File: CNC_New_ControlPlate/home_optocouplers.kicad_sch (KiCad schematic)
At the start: 17 parts

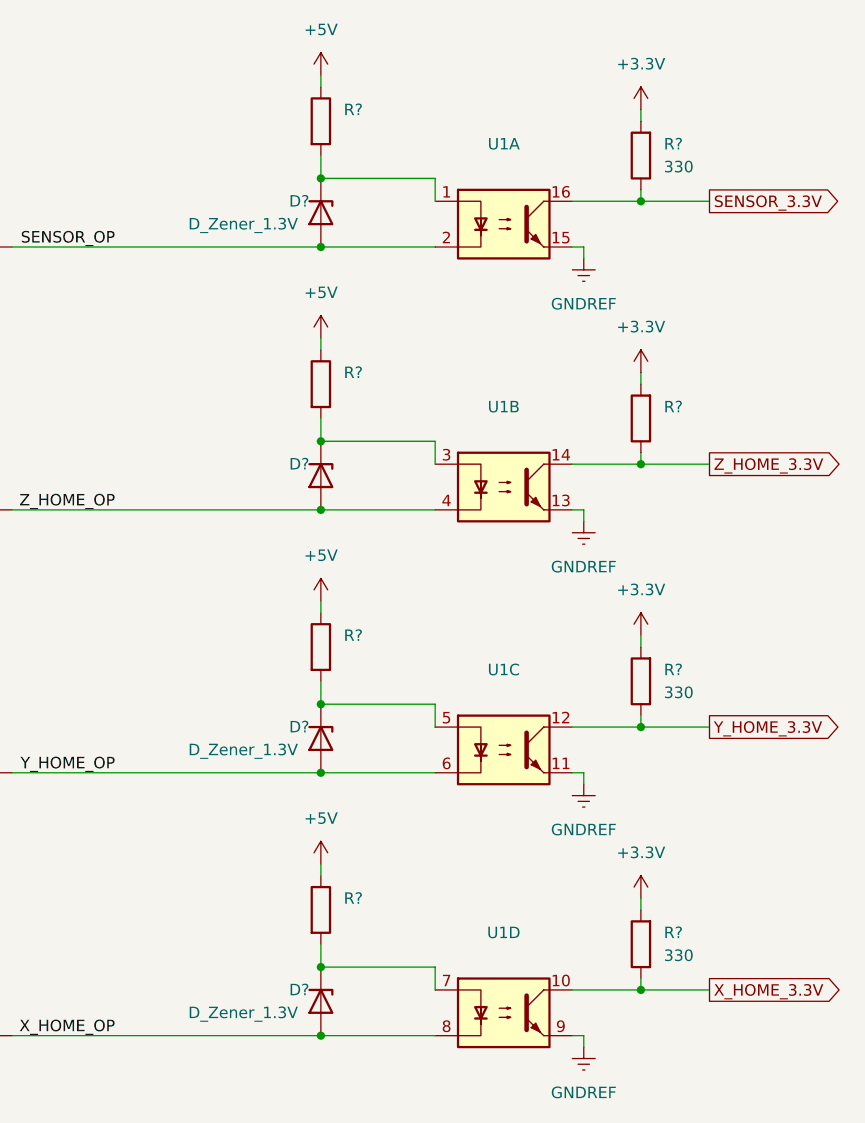
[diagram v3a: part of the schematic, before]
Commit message: Add spindel sch
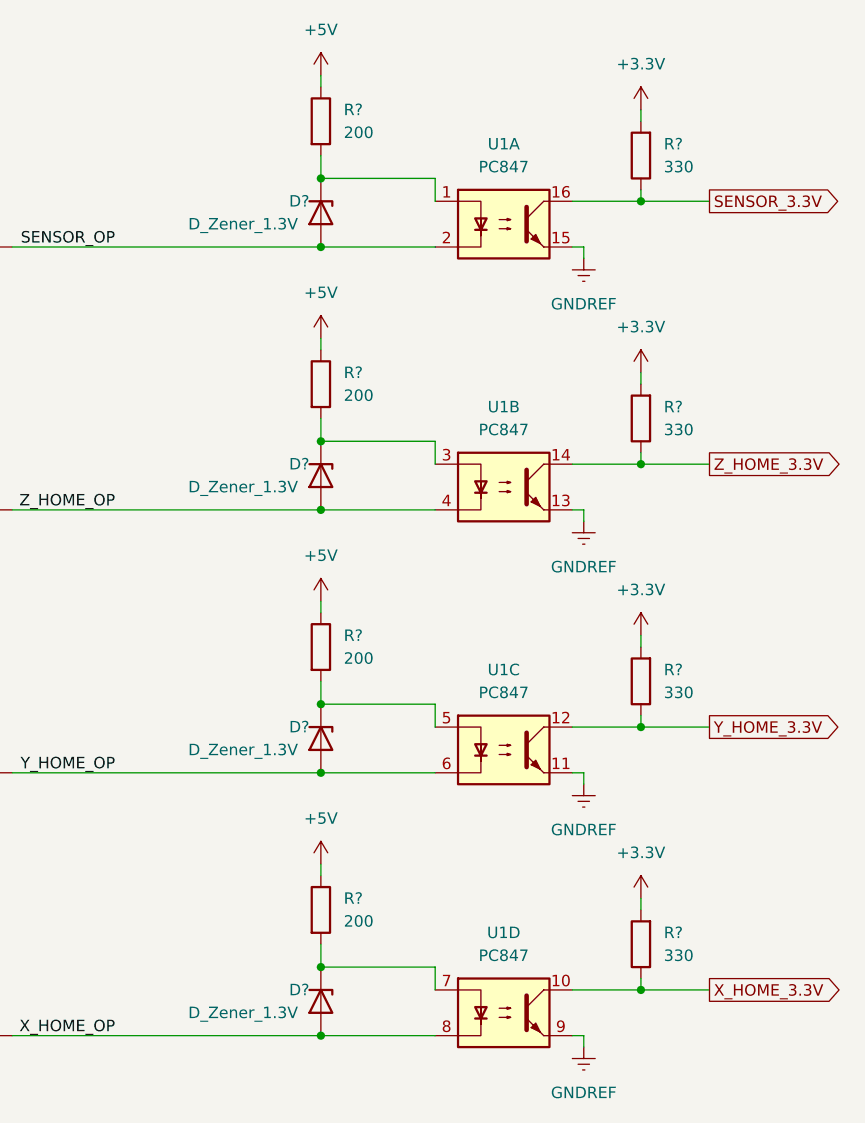
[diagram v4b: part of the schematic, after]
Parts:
- D?: value (none) -> D_Zener_1.3V; footprint (none) -> Diode_SMD:D_0603_1608Metric
- FB2: value (none) -> FerriteBead; footprint (none) -> Resistor_SMD:R_0603_1608Metric
- R? (x2): value (none) -> 200
- R? (x2): value (none) -> 200; footprint (none) -> Resistor_SMD:R_0603_1608Metric
- R?: value (none) -> 330; footprint (none) -> Resistor_SMD:R_0603_1608Metric
- U1: value (none) -> PC847; footprint (none) -> Package_DIP:DIP-16_W7.62mm_Socket_LongPads
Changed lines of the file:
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@@
       (effects (font (size 1.27 1.27)) (justify left))
     )
-    (property "Value" "" (id 1) (at 156.21 96.5199 0)
+    (property "Value" "200" (id 1) (at 156.21 96.5199 0)
       (effects (font (size 1.27 1.27)) (justify left))
     )
@@
       (effects (font (size 1.27 1.27)) (justify right))
     )
-    (property "Value" "" (id 1) (at 151.13 77.47 90)
-      (effects (font (size 1.27 1.27)) (justify right))
-    )
-    (property "Footprint" "" (id 2) (at 153.67 76.2 0)
+    (property "Value" "D_Zener_1.3V" (id 1) (at 151.13 77.47 90)
+      (effects (font (size 1.27 1.27)) (justify right))
+    )
+    (property "Footprint" "Diode_SMD:D_0603_1608Metric" (id 2) (at 153.67 76.2 0)
       (effects (font (size 1.27 1.27)) hide)
     )
@@
       (effects (font (size 1.27 1.27)) (justify left))
     )
-    (property "Value" "" (id 1) (at 156.21 38.0999 0)
-      (effects (font (size 1.27 1.27)) (justify left))
-    )
-    (property "Footprint" "" (id 2) (at 151.892 36.83 90)
+    (property "Value" "200" (id 1) (at 156.21 38.0999 0)
+      (effects (font (size 1.27 1.27)) (justify left))
+    )
+    (property "Footprint" "Resistor_SMD:R_0603_1608Metric" (id 2) (at 151.892 36.83 90)
       (effects (font (size 1.27 1.27)) hide)
     )
@@
     (in_bom yes) (on_board yes) (fields_autoplaced)
     (property "Reference" "U1" (id 0) (at 173.99 39.37 0))
-    (property "Value" "" (id 1) (at 173.99 41.91 0))
-    (property "Footprint" "" (id 2) (at 168.91 53.34 0)
+    (property "Value" "PC847" (id 1) (at 173.99 41.91 0))
+    (property "Footprint" "Package_DIP:DIP-16_W7.62mm_Socket_LongPads" (id 2) (at 168.91 53.34 0)
       (effects (font (size 1.27 1.27) italic) (justify left) hide)
     )
@@
       (effects (font (size 1.27 1.27)) (justify left))
     )
-    (property "Value" "" (id 1) (at 156.21 67.3099 0)
-      (effects (font (size 1.27 1.27)) (justify left))
-    )
-    (property "Footprint" "" (id 2) (at 151.892 66.04 90)
+    (property "Value" "200" (id 1) (at 156.21 67.3099 0)
+      (effects (font (size 1.27 1.27)) (justify left))
+    )
+    (property "Footprint" "Resistor_SMD:R_0603_1608Metric" (id 2) (at 151.892 66.04 90)
       (effects (font (size 1.27 1.27)) hide)
     )
@@
       (effects (font (size 1.27 1.27)) (justify left))
     )
-    (property "Value" "" (id 1) (at 156.21 125.7299 0)
+    (property "Value" "200" (id 1) (at 156.21 125.7299 0)
       (effects (font (size 1.27 1.27)) (justify left))
     )
@@
     (in_bom yes) (on_board yes) (fields_autoplaced)
     (property "Reference" "U1" (id 0) (at 173.99 127 0))
-    (property "Value" "" (id 1) (at 173.99 129.54 0))
-    (property "Footprint" "" (id 2) (at 168.91 140.97 0)
+    (property "Value" "PC847" (id 1) (at 173.99 129.54 0))
+    (property "Footprint" "Package_DIP:DIP-16_W7.62mm_Socket_LongPads" (id 2) (at 168.91 140.97 0)
       (effects (font (size 1.27 1.27) italic) (justify left) hide)
     )
@@
     (in_bom yes) (on_board yes)
     (property "Reference" "U1" (id 0) (at 173.99 97.79 0))
-    (property "Value" "" (id 1) (at 173.99 100.33 0))
-    (property "Footprint" "" (id 2) (at 168.91 111.76 0)
+    (property "Value" "PC847" (id 1) (at 173.99 100.33 0))
+    (property "Footprint" "Package_DIP:DIP-16_W7.62mm_Socket_LongPads" (id 2) (at 168.91 111.76 0)
       (effects (font (size 1.27 1.27) italic) (justify left) hide)
     )
@@
       (effects (font (size 1.27 1.27)) (justify right))
     )
-    (property "Value" "" (id 1) (at 191.77 71.1199 0)
-      (effects (font (size 1.27 1.27)) (justify right))
-    )
-    (property "Footprint" "" (id 2) (at 191.008 69.85 90)
+    (property "Value" "330" (id 1) (at 191.77 71.1199 0)
+      (effects (font (size 1.27 1.27)) (justify right))
+    )
+    (property "Footprint" "Resistor_SMD:R_0603_1608Metric" (id 2) (at 191.008 69.85 90)
       (effects (font (size 1.27 1.27)) hide)
     )
@@
     (in_bom yes) (on_board yes) (fields_autoplaced)
     (property "Reference" "U1" (id 0) (at 173.99 68.58 0))
-    (property "Value" "" (id 1) (at 173.99 71.12 0))
-    (property "Footprint" "" (id 2) (at 168.91 82.55 0)
+    (property "Value" "PC847" (id 1) (at 173.99 71.12 0))
+    (property "Footprint" "Package_DIP:DIP-16_W7.62mm_Socket_LongPads" (id 2) (at 168.91 82.55 0)
       (effects (font (size 1.27 1.27) italic) (justify left) hide)
     )
@@
     (in_bom yes) (on_board yes) (fields_autoplaced)
     (property "Reference" "FB2" (id 0) (at 115.6208 74.93 90))
-    (property "Value" "" (id 1) (at 115.6208 74.93 90)
-      (effects (font (size 1.27 1.27)) hide)
-    )
-    (property "Footprint" "" (id 2) (at 115.57 78.232 90)
-      (effects (font (size 1.27 1.27)) hide)
-    )
+    (property "Value" "FerriteBead" (id 1) (at 115.6208 74.93 90)
+      (effects (font (size 1.27 1.27)) hide)
+    )
+    (property "Footprint" "Resistor_SMD:R_0603_1608Metric" (id 2) (at 115.57 78.232 90)
+      (effects (font (size 1.27 1.27)) hide)
+    )

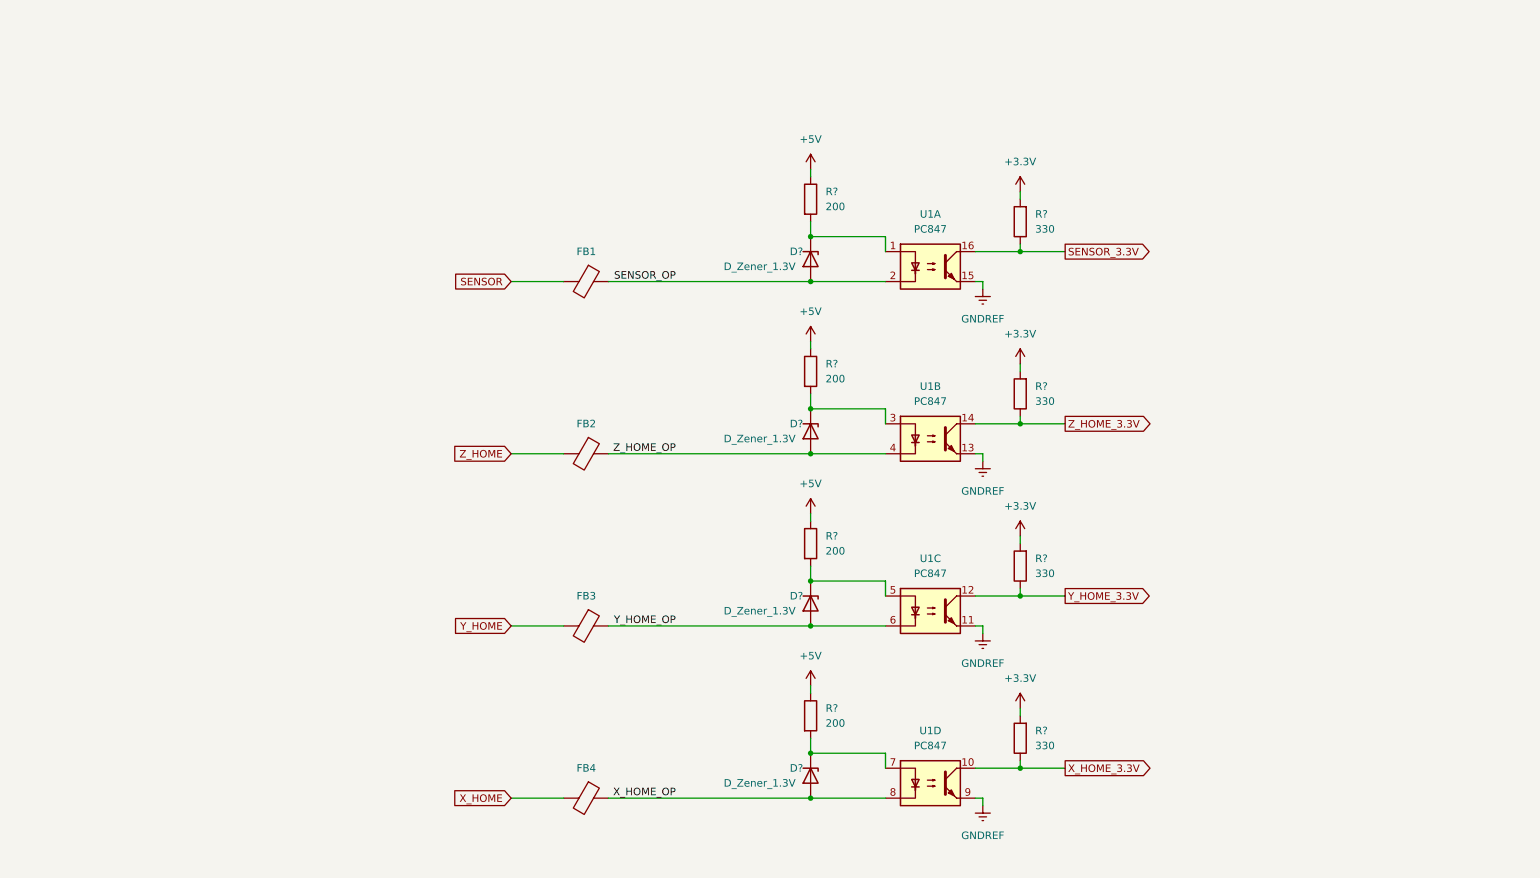
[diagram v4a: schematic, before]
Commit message: [*] номиналы блокировочных конденсаторов [+] мкроконтроллер управления оборотами шпинделя [+] кнопка паузы
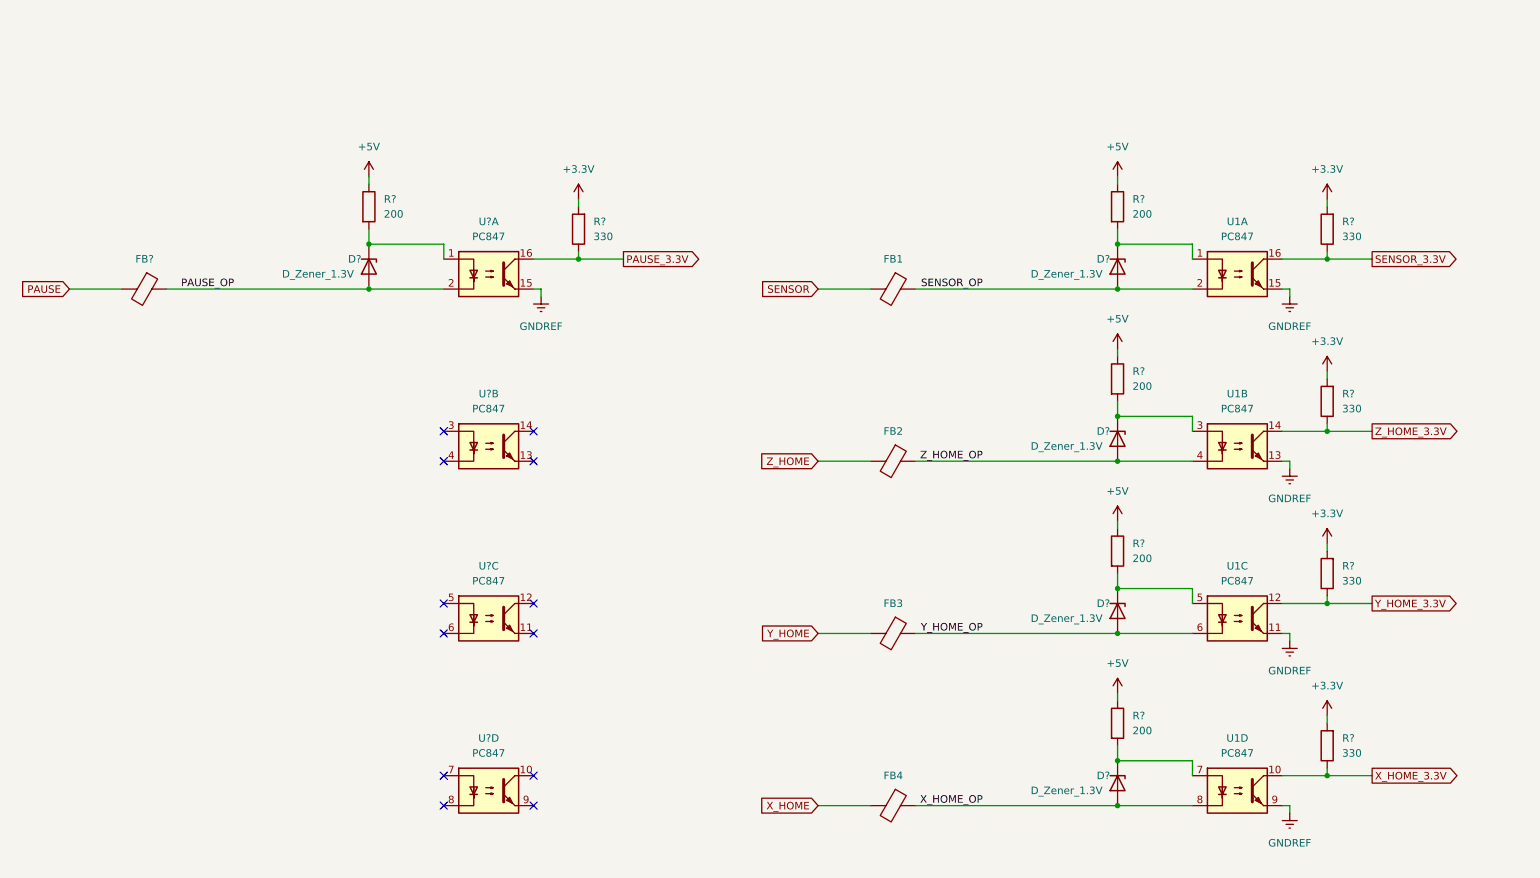
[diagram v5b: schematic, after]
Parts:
- added D?: D_Zener_1.3V, Diode_SMD:D_0603_1608Metric, symbol Device:D_Zener
- added FB?: FerriteBead, Resistor_SMD:R_0603_1608Metric, symbol Device:FerriteBead
- added R?: 330, Resistor_SMD:R_0603_1608Metric, symbol Device:R
- added R?: 200, Resistor_SMD:R_0603_1608Metric, symbol Device:R
- added U? (x4): PC847, Package_DIP:DIP-16_W7.62mm_Socket_LongPads, symbol Isolator:PC847
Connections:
- net +3V3: now also R?.2
- net +5V: now also R?.1
- net GNDREF: now also U?.15
- new net: D?.1 (K), R?.2, U?.1
- new net PAUSE: FB?.2
- new net PAUSE_3.3V: R?.1, U?.16
- new net PAUSE_OP: D?.2 (A), FB?.1, U?.2
- no-connect marks 0 -> 12
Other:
- moved on the sheet: D?, FB1, FB2, FB3, FB4, R?, U1A, U1B, U1C, U1D
